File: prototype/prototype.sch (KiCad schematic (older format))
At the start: 31 parts, among them P1 CONN_25X2, P2 CONN_25X2, P3 VGACONN, U1 MC68SEC000

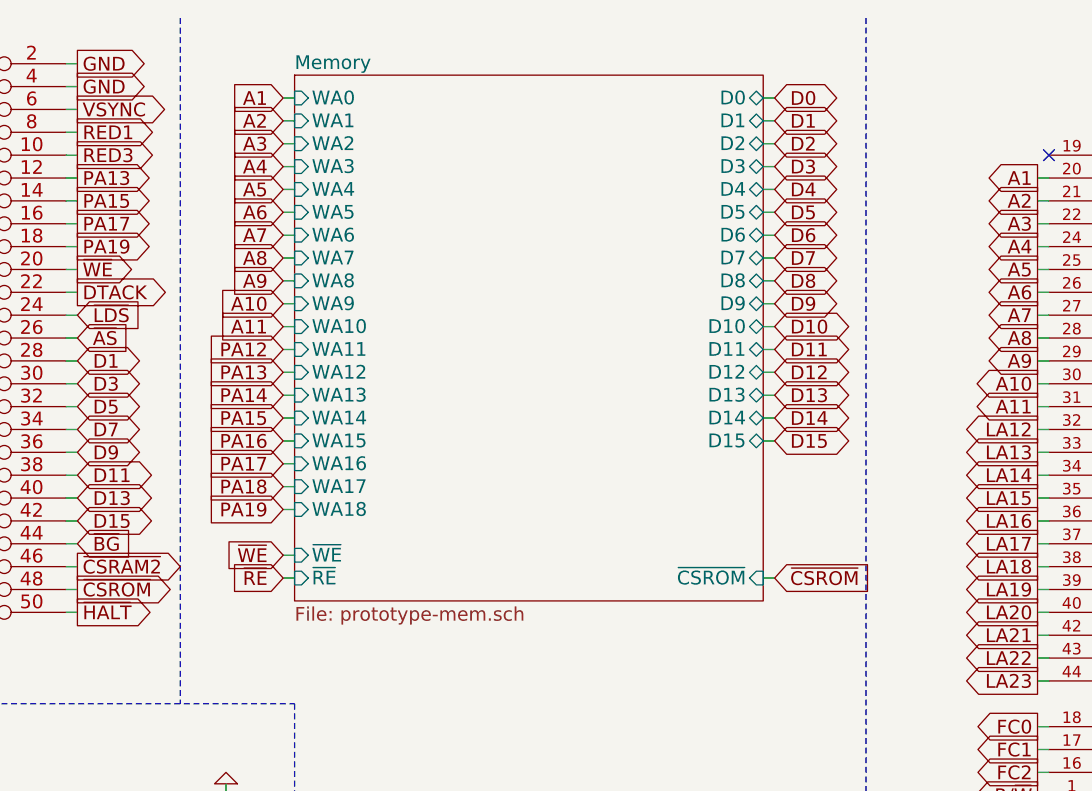
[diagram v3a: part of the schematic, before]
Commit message: Add placeholders for the RAM chip-selects.
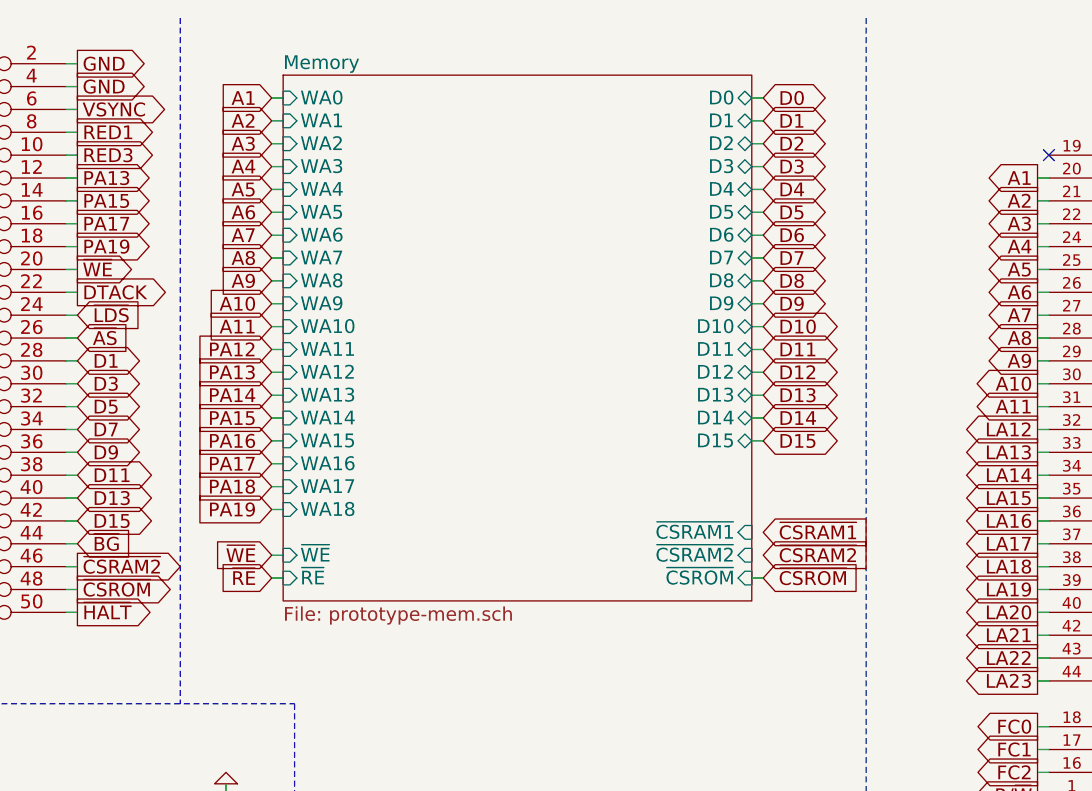
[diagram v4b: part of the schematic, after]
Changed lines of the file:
@@
 Wire Wire Line
 	4050 4800 4100 4800
-Text GLabel 7300 3050 2    60   Input ~ 0
+Text GLabel 7250 3050 2    60   Input ~ 0
 ~CSROM
-Text GLabel 7300 950  2    60   BiDi ~ 0
+Text GLabel 7250 950  2    60   BiDi ~ 0
 D0
-Text GLabel 7300 1050 2    60   BiDi ~ 0
+Text GLabel 7250 1050 2    60   BiDi ~ 0
 D1
-Text GLabel 7300 1150 2    60   BiDi ~ 0
+Text GLabel 7250 1150 2    60   BiDi ~ 0
 D2
-Text GLabel 7300 1250 2    60   BiDi ~ 0
+Text GLabel 7250 1250 2    60   BiDi ~ 0
 D3
-Text GLabel 7300 1350 2    60   BiDi ~ 0
+Text GLabel 7250 1350 2    60   BiDi ~ 0
 D4
-Text GLabel 7300 1450 2    60   BiDi ~ 0
+Text GLabel 7250 1450 2    60   BiDi ~ 0
 D5
-Text GLabel 7300 1550 2    60   BiDi ~ 0
+Text GLabel 7250 1550 2    60   BiDi ~ 0
 D6
-Text GLabel 7300 1650 2    60   BiDi ~ 0
+Text GLabel 7250 1650 2    60   BiDi ~ 0
 D7
-Text GLabel 7300 1750 2    60   BiDi ~ 0
+Text GLabel 7250 1750 2    60   BiDi ~ 0
 D8
-Text GLabel 7300 1850 2    60   BiDi ~ 0
+Text GLabel 7250 1850 2    60   BiDi ~ 0
 D9
-Text GLabel 7300 1950 2    60   BiDi ~ 0
+Text GLabel 7250 1950 2    60   BiDi ~ 0
 D10
-Text GLabel 7300 2050 2    60   BiDi ~ 0
+Text GLabel 7250 2050 2    60   BiDi ~ 0
 D11
-Text GLabel 7300 2150 2    60   BiDi ~ 0
+Text GLabel 7250 2150 2    60   BiDi ~ 0
 D12
-Text GLabel 7300 2250 2    60   BiDi ~ 0
+Text GLabel 7250 2250 2    60   BiDi ~ 0
 D13
-Text GLabel 7300 2350 2    60   BiDi ~ 0
+Text GLabel 7250 2350 2    60   BiDi ~ 0
 D14
-Text GLabel 7300 2450 2    60   BiDi ~ 0
+Text GLabel 7250 2450 2    60   BiDi ~ 0
 D15
 $Comp
@@
 Wire Wire Line
 	4200 1600 4250 1600
-Text GLabel 5150 950  0    60   Input ~ 0
+Text GLabel 5100 950  0    60   Input ~ 0
 A1
-Text GLabel 5150 1050 0    60   Input ~ 0
+Text GLabel 5100 1050 0    60   Input ~ 0
 A2
-Text GLabel 5150 1150 0    60   Input ~ 0
+Text GLabel 5100 1150 0    60   Input ~ 0
 A3
-Text GLabel 5150 1250 0    60   Input ~ 0
+Text GLabel 5100 1250 0    60   Input ~ 0
 A4
-Text GLabel 5150 1350 0    60   Input ~ 0
+Text GLabel 5100 1350 0    60   Input ~ 0
 A5
-Text GLabel 5150 1450 0    60   Input ~ 0
+Text GLabel 5100 1450 0    60   Input ~ 0
 A6
-Text GLabel 5150 1550 0    60   Input ~ 0
+Text GLabel 5100 1550 0    60   Input ~ 0
 A7
-Text GLabel 5150 1650 0    60   Input ~ 0
+Text GLabel 5100 1650 0    60   Input ~ 0
 A8
-Text GLabel 5150 1750 0    60   Input ~ 0
+Text GLabel 5100 1750 0    60   Input ~ 0
 A9
-Text GLabel 5150 1850 0    60   Input ~ 0
+Text GLabel 5100 1850 0    60   Input ~ 0
 A10
-Text GLabel 5150 1950 0    60   Input ~ 0
+Text GLabel 5100 1950 0    60   Input ~ 0
 A11
-Text GLabel 5150 2050 0    60   Input ~ 0
+Text GLabel 5100 2050 0    60   Input ~ 0
 PA12
-Text GLabel 5150 2150 0    60   Input ~ 0
+Text GLabel 5100 2150 0    60   Input ~ 0
 PA13
-Text GLabel 5150 2250 0    60   Input ~ 0
+Text GLabel 5100 2250 0    60   Input ~ 0
 PA14
-Text GLabel 5150 2350 0    60   Input ~ 0
+Text GLabel 5100 2350 0    60   Input ~ 0
 PA15
-Text GLabel 5150 2450 0    60   Input ~ 0
+Text GLabel 5100 2450 0    60   Input ~ 0
 PA16
-Text GLabel 5150 2550 0    60   Input ~ 0
+Text GLabel 5100 2550 0    60   Input ~ 0
 PA17
-Text GLabel 5150 2650 0    60   Input ~ 0
+Text GLabel 5100 2650 0    60   Input ~ 0
 PA18
-Text GLabel 5150 2750 0    60   Input ~ 0
+Text GLabel 5100 2750 0    60   Input ~ 0
 PA19
 $Sheet
-S 5200 850  2050 2300
+S 5150 850  2050 2300
 U 551A40FD
 F0 "Memory" 60
 F1 "prototype-mem.sch" 60
-F2 "WA0" I L 5200 950 60
-F3 "WA1" I L 5200 1050 60
-F4 "WA2" I L 5200 1150 60
-F5 "WA3" I L 5200 1250 60
-F6 "WA4" I L 5200 1350 60
-F7 "WA5" I L 5200 1450 60
-F8 "WA6" I L 5200 1550 60
-F9 "WA7" I L 5200 1650 60
-F10 "WA8" I L 5200 1750 60
-F11 "WA9" I L 5200 1850 60
-F12 "WA10" I L 5200 1950 60
-F13 "WA11" I L 5200 2050 60
-F14 "WA12" I L 5200 2150 60
-F15 "WA13" I L 5200 2250 60
-F16 "WA14" I L 5200 2350 60
-F17 "WA15" I L 5200 2450 60
-F18 "WA16" I L 5200 2550 60
-F19 "WA17" I L 5200 2650 60
-F20 "WA18" I L 5200 2750 60
-F21 "D0" B R 7250 950 60
-F22 "D1" B R 7250 1050 60
-F23 "D2" B R 7250 1150 60
-F24 "D3" B R 7250 1250 60
-F25 "D4" B R 7250 1350 60
-F26 "D5" B R 7250 1450 60
-F27 "D6" B R 7250 1550 60
-F28 "D7" B R 7250 1650 60
-F29 "D8" B R 7250 1750 60
-F30 "D9" B R 7250 1850 60
-F31 "D10" B R 7250 1950 60
-F32 "D11" B R 7250 2050 60
-F33 "D12" B R 7250 2150 60
-F34 "D13" B R 7250 2250 60
-F35 "D14" B R 7250 2350 60
-F36 "D15" B R 7250 2450 60
-F37 "~CSROM" I R 7250 3050 60
-F38 "~WE" I L 5200 2950 60
-F39 "~RE" I L 5200 3050 60
+F2 "WA0" I L 5150 950 60
+F3 "WA1" I L 5150 1050 60
+F4 "WA2" I L 5150 1150 60
+F5 "WA3" I L 5150 1250 60
+F6 "WA4" I L 5150 1350 60
+F7 "WA5" I L 5150 1450 60
+F8 "WA6" I L 5150 1550 60
+F9 "WA7" I L 5150 1650 60
+F10 "WA8" I L 5150 1750 60
+F11 "WA9" I L 5150 1850 60
+F12 "WA10" I L 5150 1950 60
+F13 "WA11" I L 5150 2050 60
+F14 "WA12" I L 5150 2150 60
+F15 "WA13" I L 5150 2250 60
+F16 "WA14" I L 5150 2350 60
+F17 "WA15" I L 5150 2450 60
+F18 "WA16" I L 5150 2550 60
+F19 "WA17" I L 5150 2650 60
+F20 "WA18" I L 5150 2750 60
+F21 "D0" B R 7200 950 60
+F22 "D1" B R 7200 1050 60
+F23 "D2" B R 7200 1150 60
+F24 "D3" B R 7200 1250 60
+F25 "D4" B R 7200 1350 60
+F26 "D5" B R 7200 1450 60
+F27 "D6" B R 7200 1550 60
+F28 "D7" B R 7200 1650 60
+F29 "D8" B R 7200 1750 60
+F30 "D9" B R 7200 1850 60
+F31 "D10" B R 7200 1950 60
+F32 "D11" B R 7200 2050 60
+F33 "D12" B R 7200 2150 60
+F34 "D13" B R 7200 2250 60
+F35 "D14" B R 7200 2350 60
+F36 "D15" B R 7200 2450 60
+F37 "~CSROM" I R 7200 3050 60
+F38 "~WE" I L 5150 2950 60
+F39 "~RE" I L 5150 3050 60
+F40 "~CSRAM1" I R 7200 2850 60
+F41 "~CSRAM2" I R 7200 2950 60
 $EndSheet
 Wire Wire Line
-	5150 950  5200 950
-Wire Wire Line
-	5150 1050 5200 1050
-Wire Wire Line
-	5150 1150 5200 1150
-Wire Wire Line
-	5150 1250 5200 1250
-Wire Wire Line
-	5150 1350 5200 1350
-Wire Wire Line
-	5150 1450 5200 1450
-Wire Wire Line
-	5150 1550 5200 1550
-Wire Wire Line
-	5150 1650 5200 1650
-Wire Wire Line
-	5150 1750 5200 1750
-Wire Wire Line
-	5150 1850 5200 1850
-Wire Wire Line
-	5150 1950 5200 1950
-Wire Wire Line
-	5150 2050 5200 2050
-Wire Wire Line
-	5150 2150 5200 2150
-Wire Wire Line
-	5150 2250 5200 2250
-Wire Wire Line
-	5150 2350 5200 2350
-Wire Wire Line
-	5150 2450 5200 2450
-Wire Wire Line
-	5150 2550 5200 2550
-Wire Wire Line
-	5150 2650 5200 2650
-Wire Wire Line
-	5150 2750 5200 2750
-Wire Wire Line
-	7250 950  7300 950
-Wire Wire Line
-	7250 1050 7300 1050
-Wire Wire Line
-	7250 1150 7300 1150
-Wire Wire Line
-	7250 1250 7300 1250
-Wire Wire Line
-	7250 1350 7300 1350
-Wire Wire Line
-	7250 1450 7300 1450
-Wire Wire Line
-	7250 1550 7300 1550
-Wire Wire Line
-	7250 1650 7300 1650
-Wire Wire Line
-	7250 1750 7300 1750
-Wire Wire Line
-	7250 1850 7300 1850
-Wire Wire Line
-	7250 1950 7300 1950
-Wire Wire Line
-	7250 2050 7300 2050
-Wire Wire Line
-	7250 2150 7300 2150
-Wire Wire Line
-	7250 2250 7300 2250
-Wire Wire Line
-	7250 2350 7300 2350
-Wire Wire Line
-	7250 2450 7300 2450
+	5100 950  5150 950
+Wire Wire Line
+	5100 1050 5150 1050
+Wire Wire Line
+	5100 1150 5150 1150
+Wire Wire Line
+	5100 1250 5150 1250
+Wire Wire Line
+	5100 1350 5150 1350
+Wire Wire Line
+	5100 1450 5150 1450
+Wire Wire Line
+	5100 1550 5150 1550
+Wire Wire Line
+	5100 1650 5150 1650
+Wire Wire Line
+	5100 1750 5150 1750
+Wire Wire Line
+	5100 1850 5150 1850
+Wire Wire Line
+	5100 1950 5150 1950
+Wire Wire Line
+	5100 2050 5150 2050
+Wire Wire Line
+	5100 2150 5150 2150
+Wire Wire Line
+	5100 2250 5150 2250
+Wire Wire Line
+	5100 2350 5150 2350
+Wire Wire Line
+	5100 2450 5150 2450
+Wire Wire Line
+	5100 2550 5150 2550
+Wire Wire Line
+	5100 2650 5150 2650
+Wire Wire Line
+	5100 2750 5150 2750
+Wire Wire Line
+	7200 950  7250 950
+Wire Wire Line
+	7200 1050 7250 1050
+Wire Wire Line
+	7200 1150 7250 1150
+Wire Wire Line
+	7200 1250 7250 1250
+Wire Wire Line
+	7200 1350 7250 1350
+Wire Wire Line
+	7200 1450 7250 1450
+Wire Wire Line
+	7200 1550 7250 1550
+Wire Wire Line
+	7200 1650 7250 1650
+Wire Wire Line
+	7200 1750 7250 1750
+Wire Wire Line
+	7200 1850 7250 1850
+Wire Wire Line
+	7200 1950 7250 1950
+Wire Wire Line
+	7200 2050 7250 2050
+Wire Wire Line
+	7200 2150 7250 2150
+Wire Wire Line
+	7200 2250 7250 2250
+Wire Wire Line
+	7200 2350 7250 2350
+Wire Wire Line
+	7200 2450 7250 2450
 Text GLabel 3350 1700 0    60   Output ~ 0
 ~RE
@@
 Wire Wire Line
 	4200 1700 4250 1700
-Text GLabel 5150 3050 0    60   Input ~ 0
+Text GLabel 5100 3050 0    60   Input ~ 0
 ~RE
-Text GLabel 5150 2950 0    60   Input ~ 0
+Text GLabel 5100 2950 0    60   Input ~ 0
 ~WE
 Wire Wire Line
-	5150 2950 5200 2950
-Wire Wire Line
-	5150 3050 5200 3050
-Wire Wire Line
-	7250 3050 7300 3050
+	5100 2950 5150 2950
+Wire Wire Line
+	5100 3050 5150 3050
+Wire Wire Line
+	7200 3050 7250 3050
+Text GLabel 7250 2850 2    60   Input ~ 0
+~CSRAM1
+Text GLabel 7250 2950 2    60   Input ~ 0
+~CSRAM2
 $EndSCHEMATC

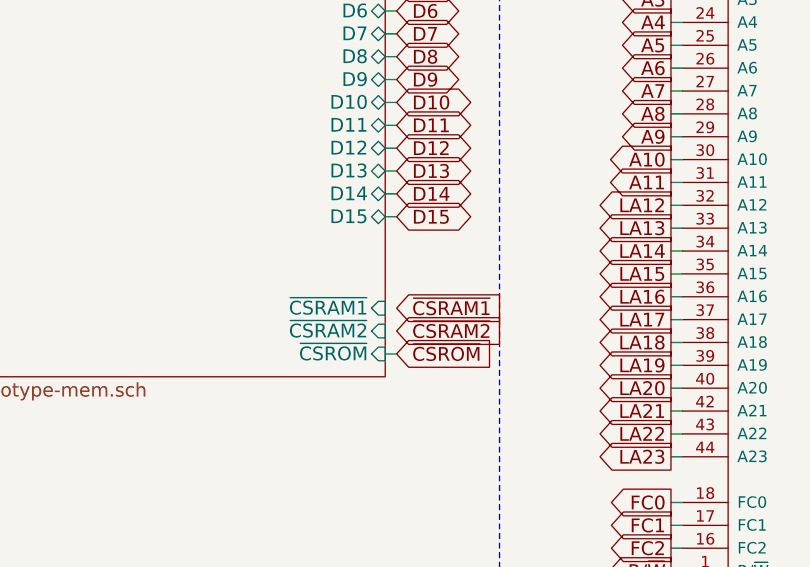
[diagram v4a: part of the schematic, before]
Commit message: RAM chip schematic.
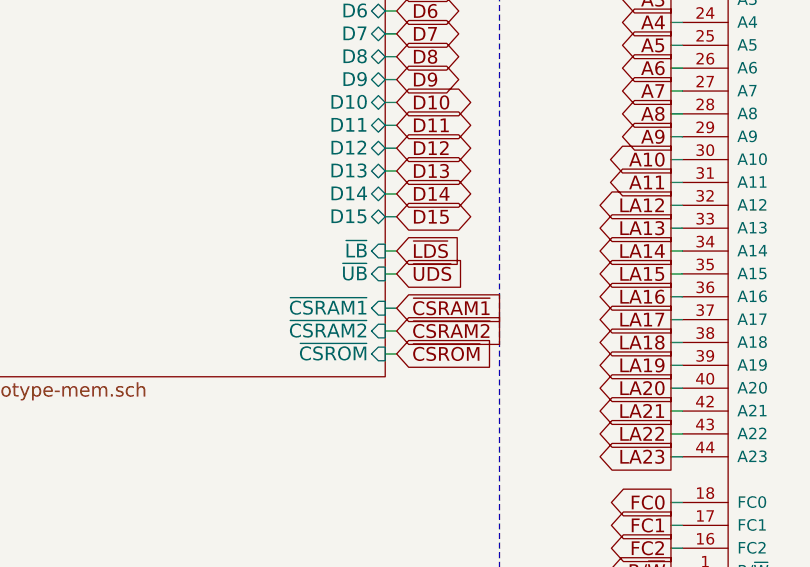
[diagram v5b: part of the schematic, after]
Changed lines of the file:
@@
 ~BR
 $Comp
-L VCC #PWR15
+L VCC #PWR14
 U 1 1 5518ED2A
 P 6400 7400
-F 0 "#PWR15" H 6400 7500 30  0001 C CNN
+F 0 "#PWR14" H 6400 7500 30  0001 C CNN
 F 1 "VCC" H 6400 7500 30  0000 C CNN
 F 2 "" H 6400 7400 60  0000 C CNN
@@
 $EndComp
 $Comp
-L GND #PWR17
+L GND #PWR15
 U 1 1 5518ED53
 P 6650 7600
-F 0 "#PWR17" H 6650 7600 30  0001 C CNN
+F 0 "#PWR15" H 6650 7600 30  0001 C CNN
 F 1 "GND" H 6650 7530 30  0001 C CNN
 F 2 "" H 6650 7600 60  0000 C CNN
@@
 GND
 $Comp
-L VCC #PWR18
+L VCC #PWR16
 U 1 1 5518EEAA
 P 9400 750
-F 0 "#PWR18" H 9400 850 30  0001 C CNN
+F 0 "#PWR16" H 9400 850 30  0001 C CNN
 F 1 "VCC" H 9400 850 30  0000 C CNN
 F 2 "" H 9400 750 60  0000 C CNN
@@
 $EndComp
 $Comp
-L GND #PWR19
+L GND #PWR17
 U 1 1 5518EFE0
 P 9400 4950
-F 0 "#PWR19" H 9400 4950 30  0001 C CNN
+F 0 "#PWR17" H 9400 4950 30  0001 C CNN
 F 1 "GND" H 9400 4880 30  0001 C CNN
 F 2 "" H 9400 4950 60  0000 C CNN
@@
 $EndComp
 $Comp
-L VCC #PWR22
+L VCC #PWR20
 U 1 1 55190866
 P 10950 3400
-F 0 "#PWR22" H 10950 3500 30  0001 C CNN
+F 0 "#PWR20" H 10950 3500 30  0001 C CNN
 F 1 "VCC" H 10950 3500 30  0000 C CNN
 F 2 "" H 10950 3400 60  0000 C CNN
@@
 $EndComp
 $Comp
-L VCC #PWR20
+L VCC #PWR18
 U 1 1 551911CA
 P 9400 5350
-F 0 "#PWR20" H 9400 5450 30  0001 C CNN
+F 0 "#PWR18" H 9400 5450 30  0001 C CNN
 F 1 "VCC" H 9400 5450 30  0000 C CNN
 F 2 "" H 9400 5350 60  0000 C CNN
@@
 $EndComp
 $Comp
-L GND #PWR21
+L GND #PWR19
 U 1 1 551911E5
 P 9400 6150
-F 0 "#PWR21" H 9400 6150 30  0001 C CNN
+F 0 "#PWR19" H 9400 6150 30  0001 C CNN
 F 1 "GND" H 9400 6080 30  0001 C CNN
 F 2 "" H 9400 6150 60  0000 C CNN
@@
 F40 "~CSRAM1" I R 7200 2850 60
 F41 "~CSRAM2" I R 7200 2950 60
+F42 "~LB" I R 7200 2600 60
+F43 "~UB" I R 7200 2700 60
 $EndSheet
 Wire Wire Line
@@
 Text GLabel 7250 2950 2    60   Input ~ 0
 ~CSRAM2
+Text GLabel 7250 2600 2    60   Input ~ 0
+~LDS
+Text GLabel 7250 2700 2    60   Input ~ 0
+~UDS
+Wire Wire Line
+	7200 2950 7250 2950
+Wire Wire Line
+	7200 2850 7250 2850
+Wire Wire Line
+	7200 2700 7250 2700
+Wire Wire Line
+	7200 2600 7250 2600
 $EndSCHEMATC

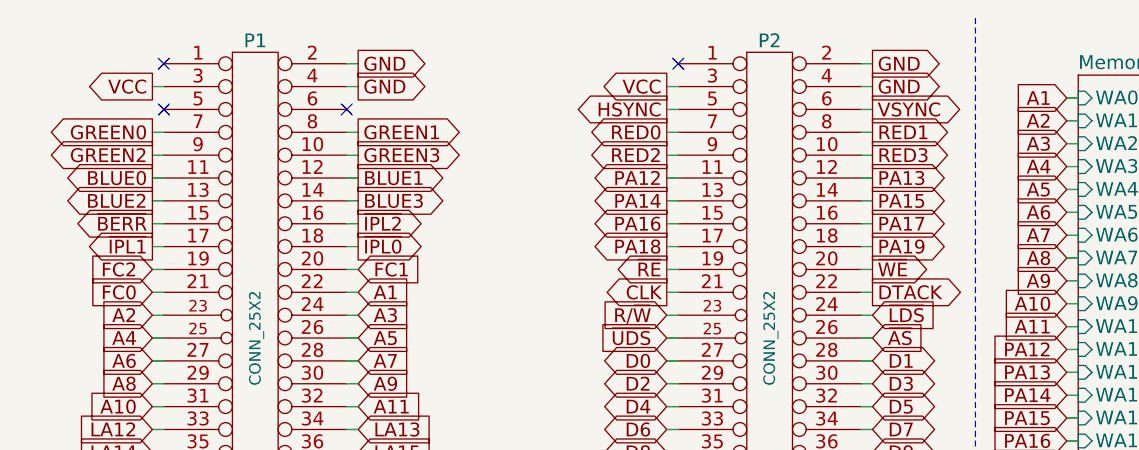
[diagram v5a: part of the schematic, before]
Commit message: Rearrange the digital color outputs for more convenient routing.
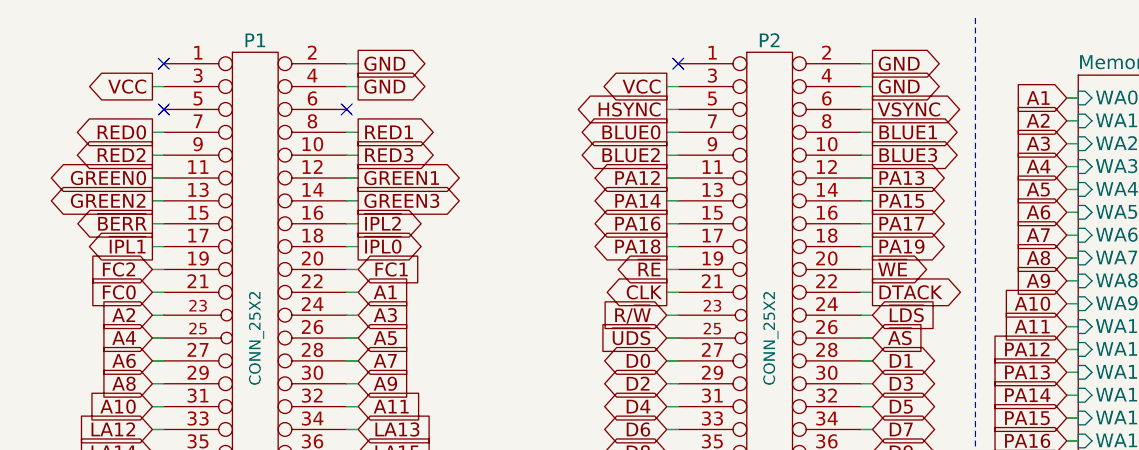
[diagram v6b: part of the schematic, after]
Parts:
- C1, C2, C3, C4: footprint (none) -> Capacitors_SMD:C_0805_HandSoldering
- D1, D10, D2, D3, D4, D5, D6, D7, D8, D9: footprint (none) -> Diodes_SMD:Diode_SOT23_Handsoldering
- P1, P2: footprint (none) -> Pin_Headers:Pin_Header_Straight_2x25
- P3: footprint (none) -> 68k-computer:DB_15F-VGA
- R1, R10, R11, R12, R13, R2, R3, R4, R5, R6, R7, R8, R9: footprint (none) -> Resistors_SMD:R_0805_HandSoldering
- U1: footprint (none) -> QFP:LQFP-64_14x14mm_Pitch0.8mm
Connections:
- net BLUE0: now also P2.7 (P7); no longer P1.11 (P11)
- net BLUE1: now also P2.8 (P8); no longer P1.12 (P12)
- net BLUE2: now also P2.9 (P9); no longer P1.13 (P13)
- net BLUE3: now also P2.10 (P10); no longer P1.14 (P14)
- net GREEN0: now also P1.11 (P11); no longer P1.7 (P7)
- net GREEN1: now also P1.12 (P12); no longer P1.8 (P8)
- net GREEN2: now also P1.13 (P13); no longer P1.9 (P9)
- net GREEN3: now also P1.14 (P14); no longer P1.10 (P10)
- net RED0: now also P1.7 (P7); no longer P2.7 (P7)
- net RED1: now also P1.8 (P8); no longer P2.8 (P8)
- net RED2: now also P1.9 (P9); no longer P2.9 (P9)
- net RED3: now also P1.10 (P10); no longer P2.10 (P10)

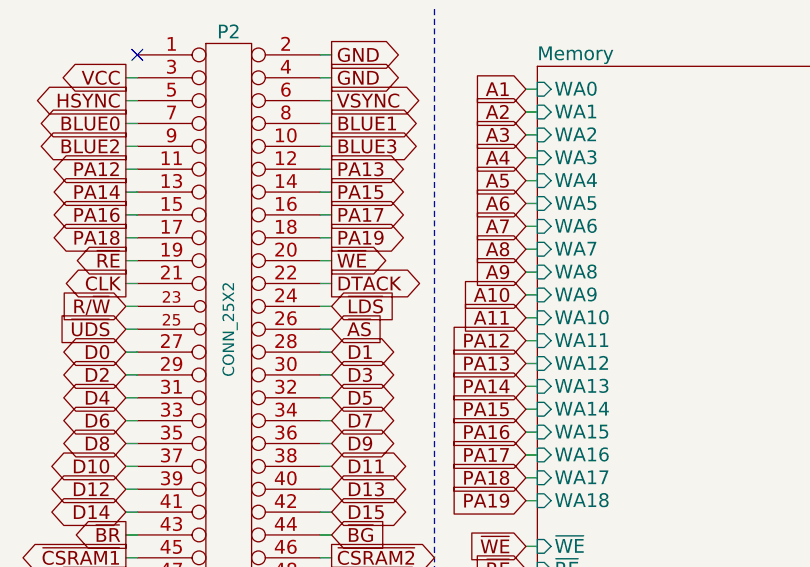
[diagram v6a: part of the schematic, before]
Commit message: DTACK label should actually be ~DTACK.
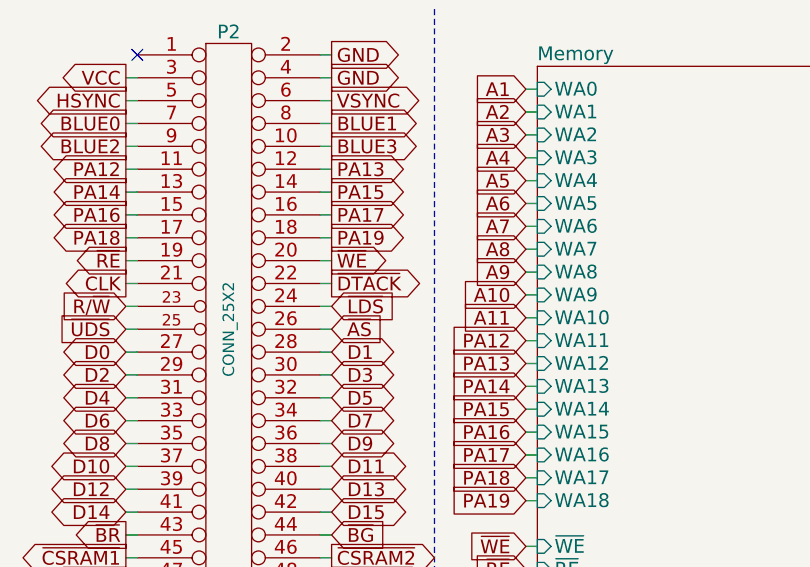
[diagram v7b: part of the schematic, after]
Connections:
- net DTACK is gone; now on net ~DTACK: P2.22 (P22)
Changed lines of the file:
@@
 CLK
 Text GLabel 4250 1800 2    60   Output ~ 0
-DTACK
+~DTACK
 Text GLabel 4250 1900 2    60   Input ~ 0
 ~LDS
